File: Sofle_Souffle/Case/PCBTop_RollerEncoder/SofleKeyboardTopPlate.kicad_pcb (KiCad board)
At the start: 2 copper layers, 143.3 x 111.8 mm, 11 parts, among them J1 Conn_01x05_Female, SW1 EVQWGD001

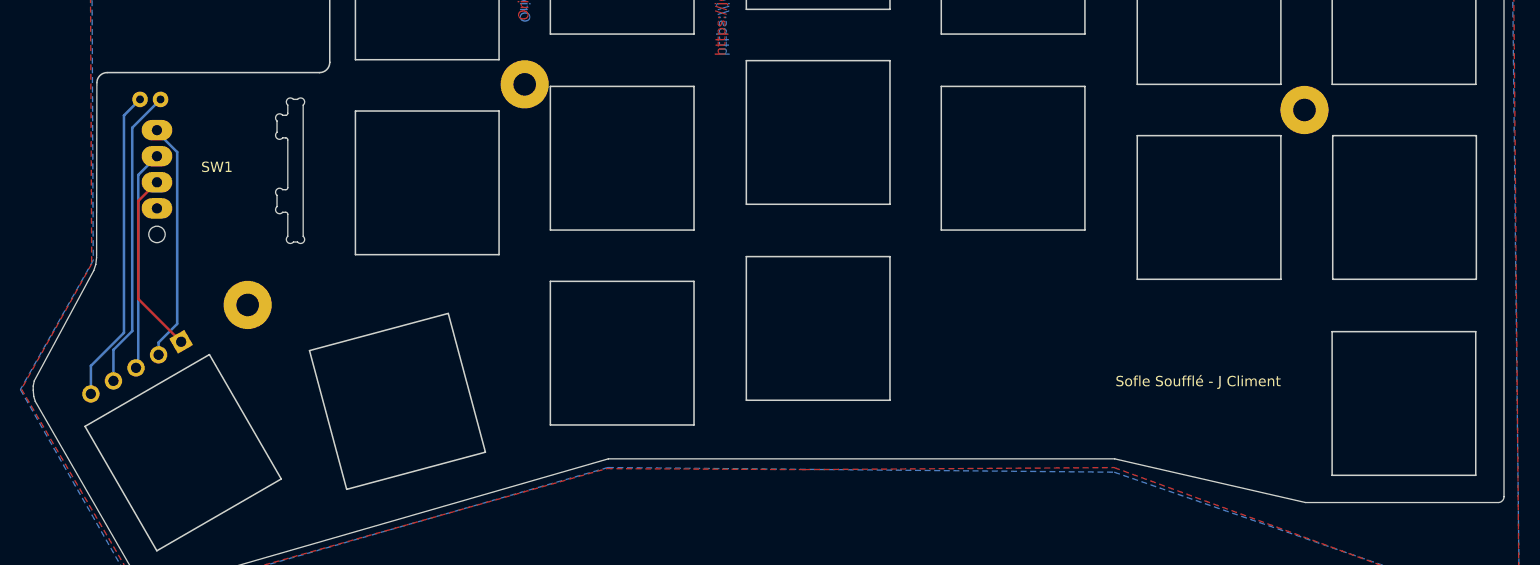
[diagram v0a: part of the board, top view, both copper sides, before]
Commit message: Moved roller encoder connectors to the same vertical location.
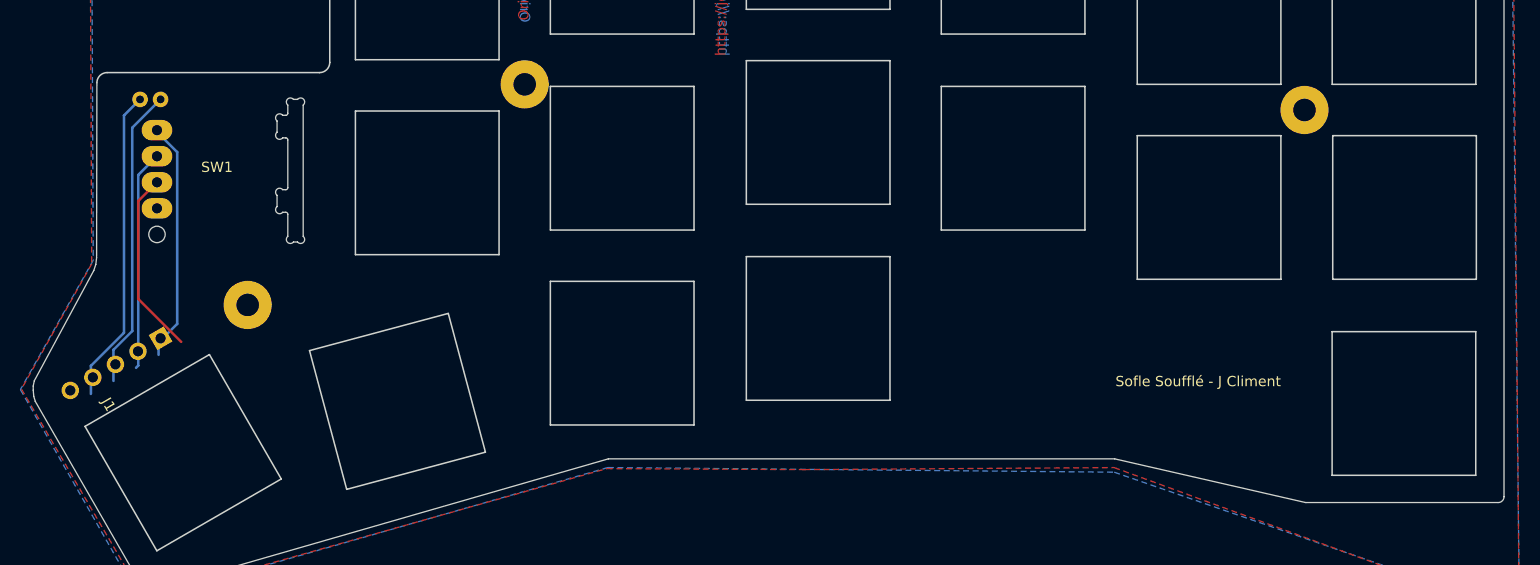
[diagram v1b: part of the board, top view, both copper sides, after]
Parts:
- J1: footprint Connector_PinHeader_2.54mm:PinHeader_1x05_P2.54mm_Horizontal -> SofleRGB:PinHeader_1x05_P2.54mm_Horizontal
- moved J1 2.04 mm to (95.5, 123.7)
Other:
- net class Default removed

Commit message: Small updates on the PCB and case.
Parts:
- added ?: , , F.Cu at (98.2, 98.7)
- added ?: , , F.Cu at (108.3, 98.7)
- added ?: , , F.Cu at (105.7, 98.7)
- added ?: , , F.Cu at (100.7, 98.7)
- added ?: , , F.Cu at (103.2, 98.7)
- added TH4: HOLE, SofleRGB:HOLE_M2_TH, F.Cu at (103.8, 120.2)
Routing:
- net ENCB: track 21.5 -> 23.8 mm
- net SWB: track 30.7 -> 32.5 mm
- net SWA: track 29.3 -> 30.9 mm
- net ENCA: track 23.5 -> 24.6 mm
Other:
- outline, holes or cut-outs redrawn

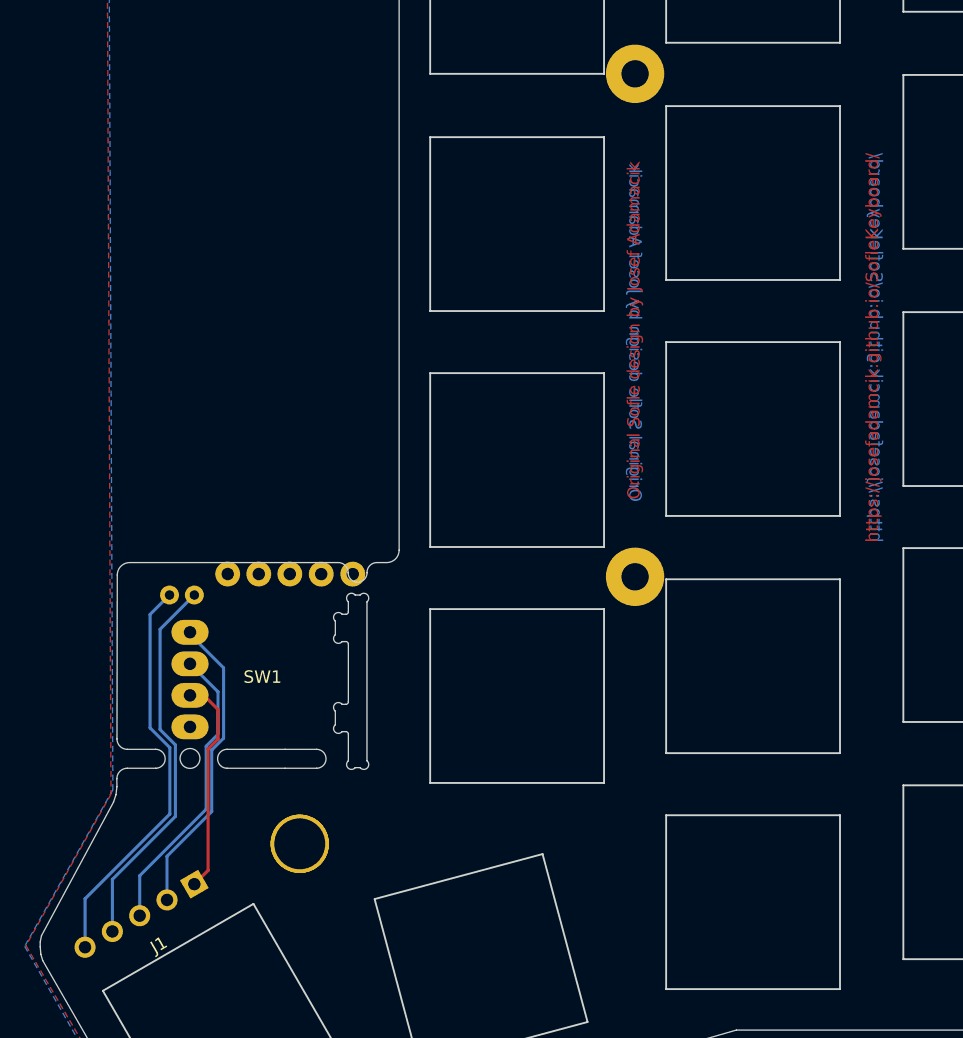
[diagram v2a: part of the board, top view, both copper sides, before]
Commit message: Completed redesign of the roller encoder pins.
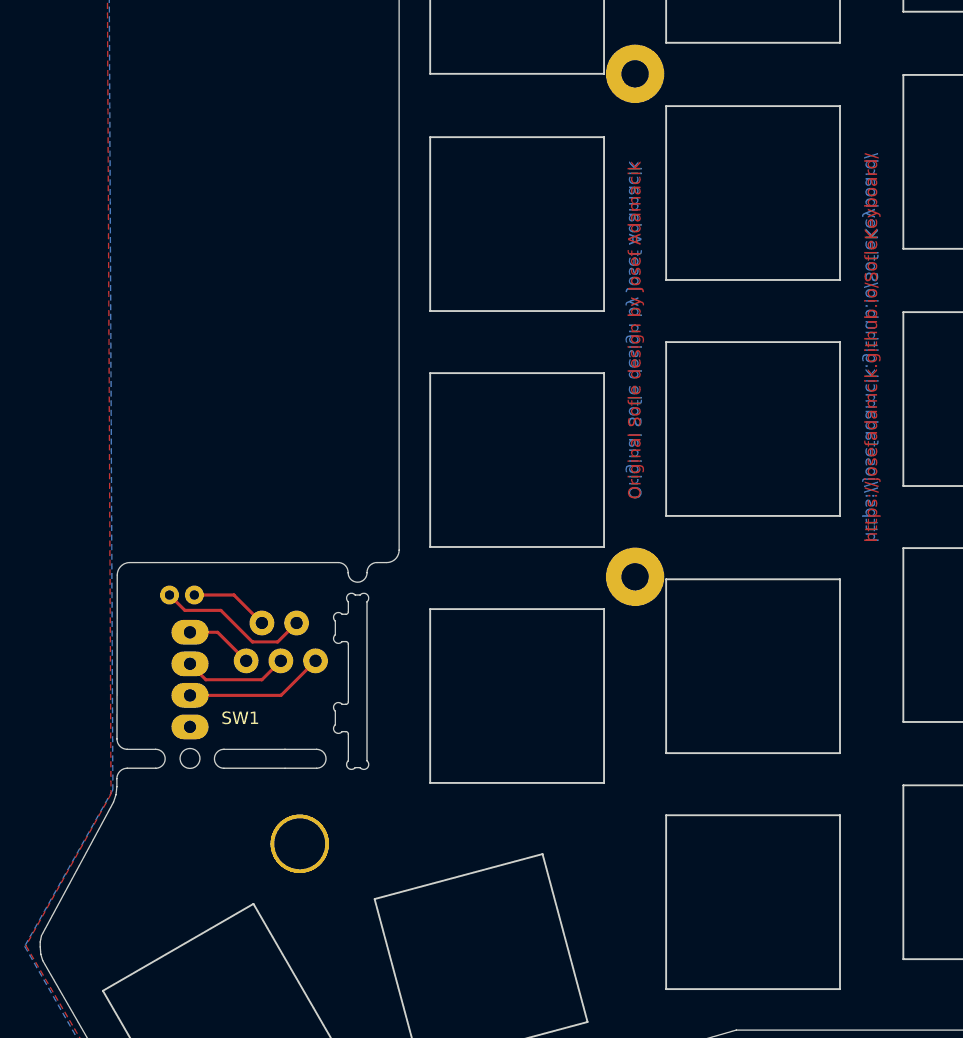
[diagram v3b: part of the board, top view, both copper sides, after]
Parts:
- removed J1: Conn_01x05_Female, SofleRGB:PinHeader_1x05_P2.54mm_Horizontal
- moved ? 8.35 mm to (105.3, 105.7)
- moved ? 8.20 mm to (102.5, 105.7)
- moved ? 7.83 mm to (99.7, 105.7)
- moved ? 6.19 mm to (100.9, 102.7)
- moved ? 6.00 mm to (103.7, 102.7)
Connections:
- ? pad 1: (no net) -> SWB
- ? pad 1: (no net) -> SWA
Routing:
- net SWA: track 30.9 -> 6.37 mm
- net SWB: track 32.5 -> 12.4 mm
- net ENCA: track 24.6 -> 5.64 mm
- net ENCB: track 23.8 -> 8.48 mm
- net GND: track 17.6 -> 11.3 mm
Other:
- outline, holes or cut-outs redrawn

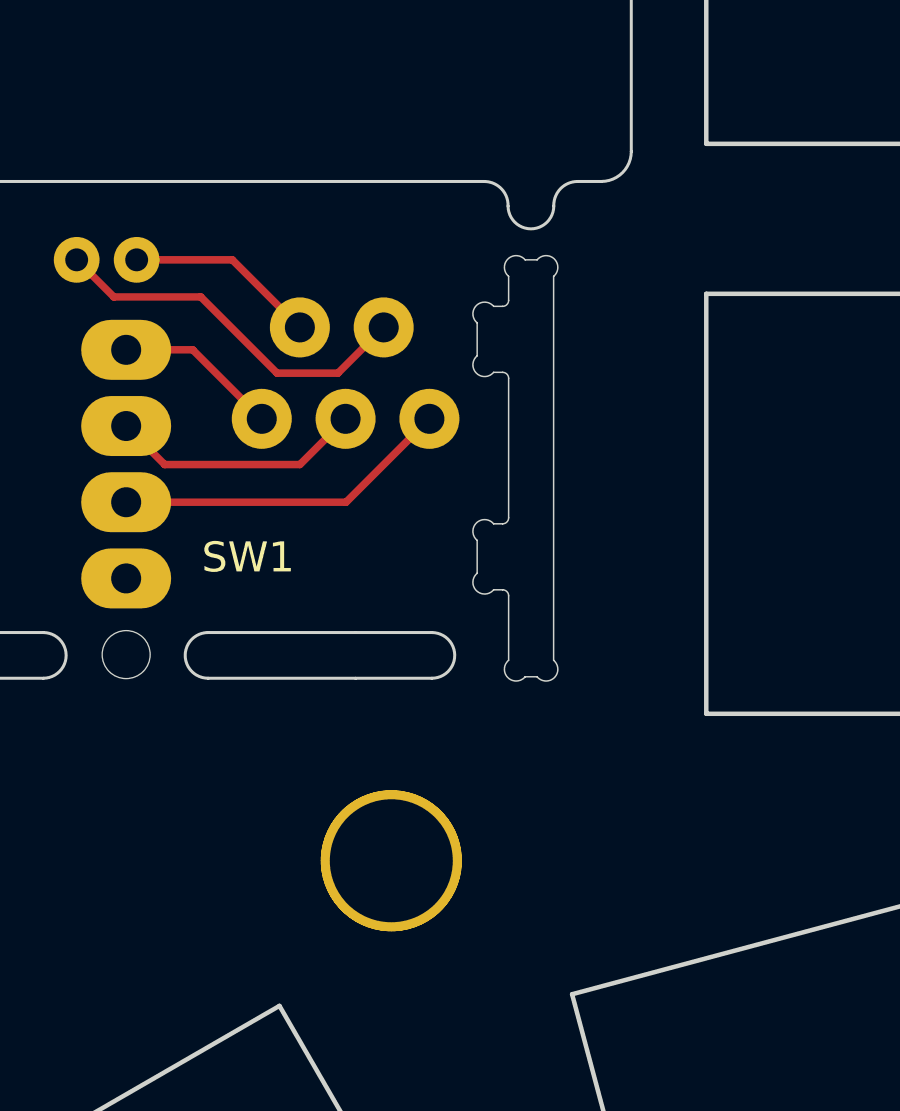
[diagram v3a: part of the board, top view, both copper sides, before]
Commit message: Fixed top case hole.
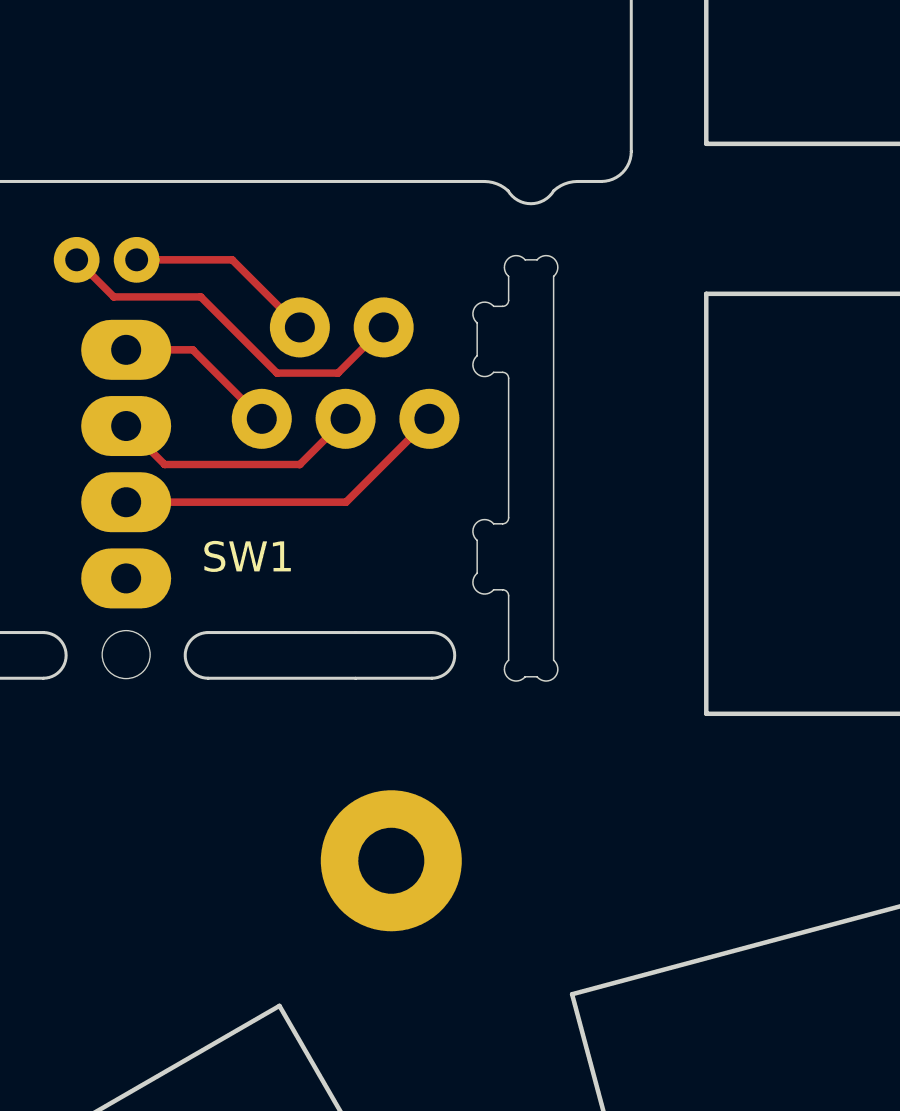
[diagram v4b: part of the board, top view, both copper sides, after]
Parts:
- removed the TH4 at (103.8, 120.2)
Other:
- outline, holes or cut-outs redrawn
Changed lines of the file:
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@@
       (net 3 "ENCB") (pinfunction "B") (pintype "passive"))
-  )
-  (footprint "SofleRGB:HOLE_M2_TH" (layer "F.Cu")
-    (at 103.77 120.17 180)
-    (property "Sheetfile" "SofleKeyboard.kicad_sch")
-    (property "Sheetname" "")
-    (attr through_hole)
-    (fp_text reference "TH4" (at 0 -2.54) (layer "F.SilkS") hide
-      (effects (font (size 0.29972 0.29972) (thickness 0.0762)))
-    )
-    (fp_text value "HOLE" (at 0 2.54) (layer "F.SilkS") hide
-      (effects (font (size 0.29972 0.29972) (thickness 0.0762)))
-    )
-    (pad "" thru_hole circle locked (at -0.225 -0.275 270) (size 4.7 4.7) (drill 4.1) (layers *.Cu *.Mask "Dwgs.User")
-      (clearance 0.3))
   )
   (footprint "" (layer "F.Cu")
@@
   (gr_line (start 152.595 115.735) (end 166.595 115.735) (layer "Edge.Cuts") (width 0.15))
   (gr_line (start 147.495 99.145) (end 147.495 113.145) (layer "Edge.Cuts") (width 0.15))
-  (gr_arc (start 109.411178 98.616822) (mid 109.635445 98.040678) (end 110.204928 97.8) (layer "Edge.Cuts") (width 0.1))
+  (gr_arc (start 109.411178 98.108822) (mid 109.779072 97.879923) (end 110.204928 97.8) (layer "Edge.Cuts") (width 0.1))
   (gr_line (start 209.695 65.745) (end 223.695 65.745) (layer "Edge.Cuts") (width 0.15))
   (gr_line (start 112.095 38.7) (end 112.295 38.4) (layer "Edge.Cuts") (width 0.1))
@@
   (gr_line (start 171.595 60.985) (end 185.595 60.985) (layer "Edge.Cuts") (width 0.15))
   (gr_line (start 166.595 96.635) (end 166.595 110.635) (layer "Edge.Cuts") (width 0.15))
-  (gr_arc (start 107.093428 97.8) (mid 107.662909 98.04068) (end 107.887178 98.616822) (layer "Edge.Cuts") (width 0.1))
-  (gr_arc (start 109.411178 98.616822) (mid 108.649178 99.378822) (end 107.887178 98.616822) (layer "Edge.Cuts") (width 0.1))
+  (gr_arc (start 107.093428 97.8) (mid 107.519282 97.879927) (end 107.887178 98.108822) (layer "Edge.Cuts") (width 0.1))
+  (gr_arc (start 109.411178 98.108822) (mid 108.649178 98.541402) (end 107.887178 98.108822) (layer "Edge.Cuts") (width 0.1))
   (gr_line (start 128.495 77.545) (end 114.495 77.545) (layer "Edge.Cuts") (width 0.15))
   (gr_line (start 128.495 115.545) (end 114.495 115.545) (layer "Edge.Cuts") (width 0.15))

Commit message: Checkpoint commit.
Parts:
- added SW1: EVQWGD001, SofleRGB:EVQWGD001, F.Cu at (75.0, 75.5)
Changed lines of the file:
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@@
       (net 2 "SWA") (pinfunction "Pin_1") (pintype "passive"))
+  )
+  (footprint "SofleRGB:EVQWGD001" (layer "F.Cu")
+    (at 75.039 75.5378)
+    (attr through_hole)
+    (fp_text reference "SW1" (at -0.25 1.35 -180) (layer "F.Fab") hide
+      (effects (font (size 1 1) (thickness 0.15)))
+    )
+    (fp_text value "EVQWGD001" (at -0.25 -3.55 -180) (layer "F.Fab") hide
+      (effects (font (size 1 1) (thickness 0.15)))
+    )
+    (fp_text user "${REFERENCE}" (at -1.783 3.317) (layer "F.SilkS")
+      (effects (font (size 1 1) (thickness 0.15)))
+    )
+    (fp_line (start 8.402987 -7.344) (end 8.402987 6.556) (layer "Dwgs.User") (width 0.15))
+    (fp_line (start -8.397013 -7.344) (end -8.397013 6.556) (layer "Dwgs.User") (width 0.15))
+    (fp_line (start -8.397013 7.293499) (end 8.402987 7.293499) (layer "Dwgs.User") (width 0.15))
+    (fp_line (start -8.397013 6.556) (end 8.402987 6.556) (layer "Dwgs.User") (width 0.15))
+    (fp_line (start -8.397013 -6.606501) (end 8.402987 -6.606501) (layer "Dwgs.User") (width 0.15))
+    (fp_line (start -8.397013 7.293499) (end -8.397013 -6.606501) (layer "Dwgs.User") (width 0.15))
+    (fp_line (start 8.402987 7.293499) (end 8.402987 -6.606501) (layer "Dwgs.User") (width 0.15))
+    (fp_line (start -8.397013 -7.344) (end 8.402987 -7.344) (layer "Dwgs.User") (width 0.15))
+    (fp_line (start 9.5 8.949499) (end -9.5 8.949499) (layer "Cmts.User") (width 0.12))
+    (fp_line (start 9.5 -9.050501) (end -9.5 -9.050501) (layer "Cmts.User") (width 0.12))
+    (fp_line (start 9.5 9) (end 9.5 -9) (layer "Cmts.User") (width 0.12))
+    (fp_line (start 9.5 -9.050501) (end 9.5 8.949499) (layer "Cmts.User") (width 0.12))
+    (fp_line (start -9.5 9) (end -9.5 -9) (layer "Cmts.User") (width 0.12))
+    (fp_line (start -9.5 -9.050501) (end -9.5 8.949499) (layer "Cmts.User") (width 0.12))
+    (fp_line (start 9.5 9) (end -9.5 9) (layer "Cmts.User") (width 0.12))
+    (fp_line (start 9.5 -9) (end -9.5 -9) (layer "Cmts.User") (width 0.12))
+    (fp_line (start 6.902987 -2.044) (end 6.902987 1.993499) (layer "Edge.Cuts") (width 0.05))
+    (fp_line (start 6.902987 -5.256501) (end 6.902988 -6.794) (layer "Edge.Cuts") (width 0.05))
+    (fp_line (start 6.702987 5.006) (end 6.402987 5.006) (layer "Edge.Cuts") (width 0.05))
+    (fp_line (start 7.453011 7.293469) (end 7.852987 7.293499) (layer "Edge.Cuts") (width 0.05))
+    (fp_line (start 7.453011 -7.34397) (end 7.852987 -7.344) (layer "Edge.Cuts") (width 0.05))
+    (fp_line (start 6.902987 5.206) (end 6.902988 6.743499) (layer "Edge.Cuts") (width 0.05))
+    (fp_line (start 8.402987 6.743499) (end 8.402987 -6.794) (layer "Edge.Cuts") (width 0.05))
+    (fp_line (start 6.702987 2.193499) (end 6.402987 2.193499) (layer "Edge.Cuts") (width 0.05))
+    (fp_line (start 5.852987 -2.794) (end 5.852987 -4.506501) (layer "Edge.Cuts") (width 0.05))
+    (fp_line (start 6.702987 -2.244) (end 6.402987 -2.244) (layer "Edge.Cuts") (width 0.05))
+    (fp_line (start 6.702987 -5.056501) (end 6.402987 -5.056501) (layer "Edge.Cuts") (width 0.05))
+    (fp_line (start 5.852987 4.456) (end 5.852987 2.743499) (layer "Edge.Cuts") (width 0.05))
+    (fp_arc (start 6.902987 -5.256501) (mid 6.844408 -5.11508) (end 6.702987 -5.056501) (layer "Edge.Cuts") (width 0.05))
+    (fp_arc (start 5.852987 2.743499) (mid 5.826853 2.167365) (end 6.402987 2.193499) (layer "Edge.Cuts") (width 0.05))
+    (fp_arc (start 6.402987 5.006) (mid 5.826853 5.032134) (end 5.852987 4.456) (layer "Edge.Cuts") (width 0.05))
+    (fp_arc (start 6.402987 -2.244) (mid 5.826853 -2.217866) (end 5.852987 -2.794) (layer "Edge.Cuts") (width 0.05))
+    (fp_arc (start 7.453011 7.293469) (mid 6.876867 7.319646) (end 6.902988 6.743499) (layer "Edge.Cuts") (width 0.05))
+    (fp_arc (start 7.852987 -7.344) (mid 8.429121 -7.370134) (end 8.402987 -6.794) (layer "Edge.Cuts") (width 0.05))
+    (fp_arc (start 6.902987 1.993499) (mid 6.844408 2.13492) (end 6.702987 2.193499) (layer "Edge.Cuts") (width 0.05))
+    (fp_arc (start 6.702987 -2.244) (mid 6.844408 -2.185421) (end 6.902987 -2.044) (layer "Edge.Cuts") (width 0.05))
+    (fp_arc (start 6.702987 5.006) (mid 6.844408 5.064579) (end 6.902987 5.206) (layer "Edge.Cuts") (width 0.05))
+    (fp_arc (start 8.402987 6.743499) (mid 8.429121 7.319633) (end 7.852987 7.293499) (layer "Edge.Cuts") (width 0.05))
+    (fp_arc (start 5.852987 -4.506501) (mid 5.826853 -5.082635) (end 6.402987 -5.056501) (layer "Edge.Cuts") (width 0.05))
+    (fp_arc (start 6.902988 -6.794) (mid 6.876867 -7.370147) (end 7.453011 -7.34397) (layer "Edge.Cuts") (width 0.05))
+    (pad "" np_thru_hole circle (at -5.847013 6.553499 90) (size 1.6 1.6) (drill 1.6) (layers *.Cu))
+    (pad "" thru_hole circle (at -5.847013 -6.604 90) (size 2 2) (drill 1.6) (layers *.Cu *.Mask))
+    (pad "" thru_hole circle (at -5.847013 6.553499 90) (size 2 2) (drill 1.6) (layers *.Cu *.Mask))
+    (pad "A" thru_hole oval (at -5.847013 -3.606501 90) (size 1.5 3) (drill 1) (layers *.Cu *.Mask))
+    (pad "A" thru_hole oval (at -5.847013 3.556 90) (size 1.5 3) (drill 1) (layers *.Cu *.Mask))
+    (pad "B" thru_hole oval (at -5.847013 -1.066501 90) (size 1.6 3) (drill 1) (layers *.Cu *.Mask))
+    (pad "B" thru_hole oval (at -5.847013 1.016 90) (size 1.6 3) (drill 1) (layers *.Cu *.Mask))
+    (pad "C" thru_hole oval (at -5.847013 1.473499 90) (size 1.6 3) (drill 1) (layers *.Cu *.Mask))
+    (pad "C" thru_hole oval (at -5.847013 -1.524 90) (size 1.6 3) (drill 1) (layers *.Cu *.Mask))
+    (pad "NC" thru_hole oval (at -5.847013 -4.064 90) (size 1.6 3) (drill 1) (layers *.Cu *.Mask))
+    (pad "NC" thru_hole oval (at -5.847013 4.013499 90) (size 1.6 3) (drill 1) (layers *.Cu *.Mask))
+    (pad "S1" thru_hole oval (at -7.747 6.553499 90) (size 1.524 2.1) (drill oval 0.762 1.1 (offset 0 -0.3)) (layers *.Cu *.Mask))
+    (pad "S1" thru_hole oval (at -7.747 -6.604 90) (size 1.524 2.1) (drill oval 0.762 1.1 (offset 0 -0.3)) (layers *.Cu *.Mask))
   )
   (footprint "" (layer "F.Cu")
